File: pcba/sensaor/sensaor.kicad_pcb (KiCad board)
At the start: 2 copper layers, 26 x 77 mm, 16 parts, among them J1 SAO, J2 WS2812, J3 Conn_01x05_Pin, J4 Conn_01x05_Pin, J5 Conn_01x05_Pin, J6 Programming, J7 Conn_01x05_Pin, J8 Conn_01x05_Pin, J9 Conn_01x05_Pin, U1 CH32V003AxMx

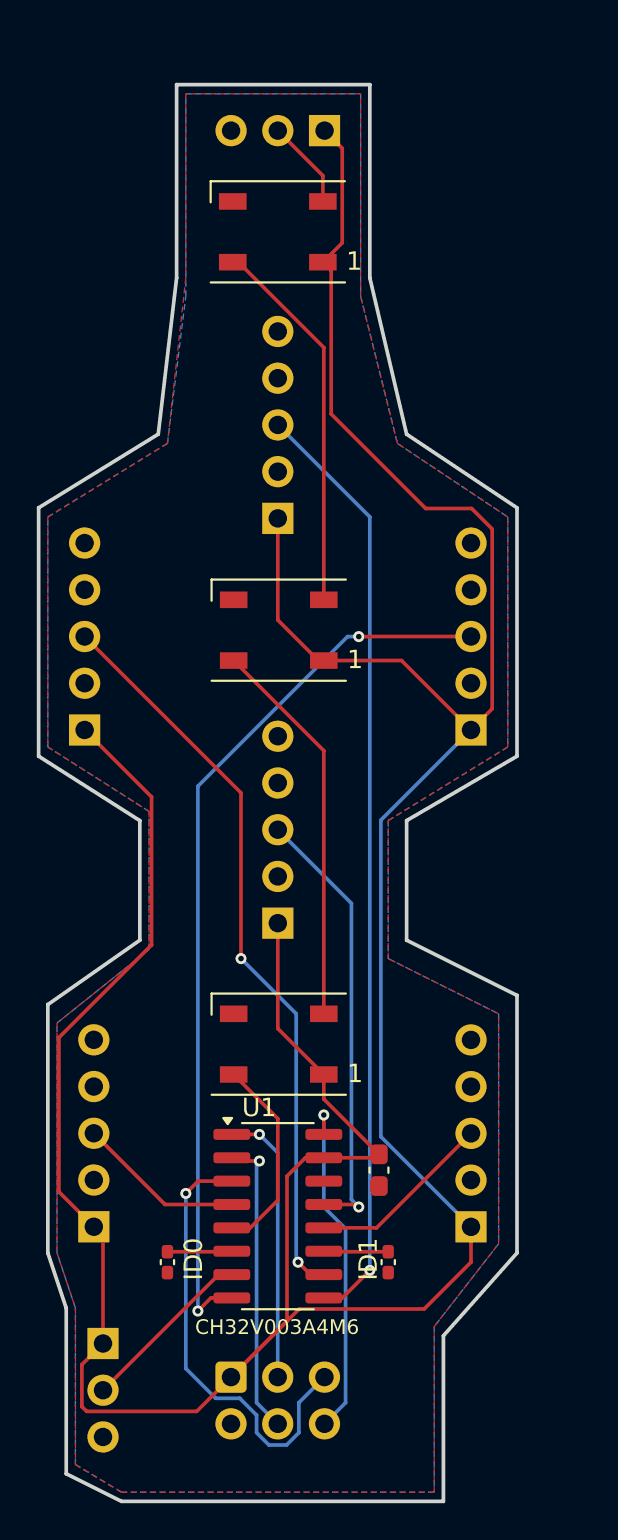
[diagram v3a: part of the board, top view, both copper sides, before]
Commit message: Add SAOAO connector, tweak some placements
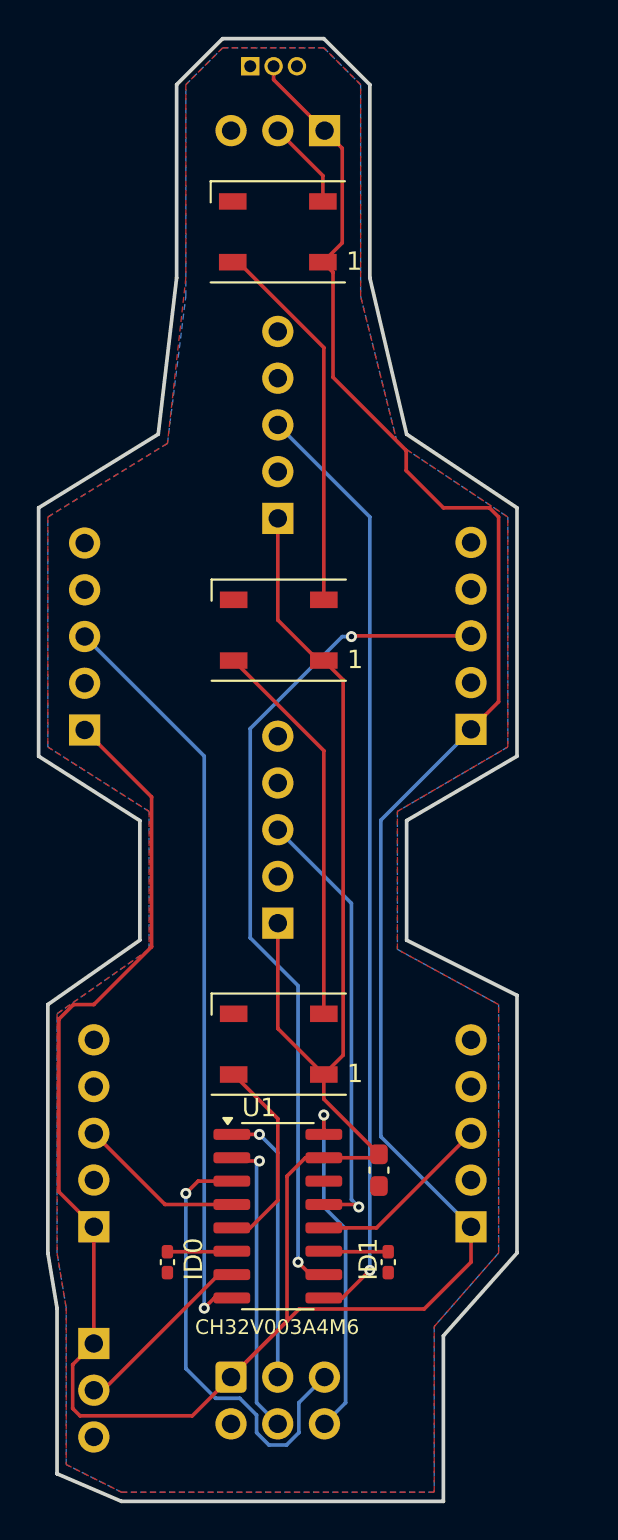
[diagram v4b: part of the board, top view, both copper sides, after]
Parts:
- added J10: SAOAO, Connector_PinHeader_1.27mm:PinHeader_1x03_P1.27mm_Vertical, B.Cu at (92.0, 17.0)
- moved J7 21.0 mm to (104.0, 53.0)
- moved J9 21.0 mm to (83.0, 53.1)
- moved J6 0.50 mm to (83.5, 86.4)
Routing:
- net VCC: track 190.5 -> 210.4 mm
- net /AB: track 48.9 -> 40.9 mm, vias 2 -> 1
- net /AR: track 40.5 -> 45.8 mm
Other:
- board size 26 x 77 mm -> 26 x 79.5 mm

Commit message: Adjustments from PCBA review
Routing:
- net VCC: track 210.4 -> 212.4 mm
- net /AR: track 45.8 -> 46.9 mm
- net Net-(D1-DOUT): track 21.2 -> 21.9 mm
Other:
- outline, holes or cut-outs redrawn

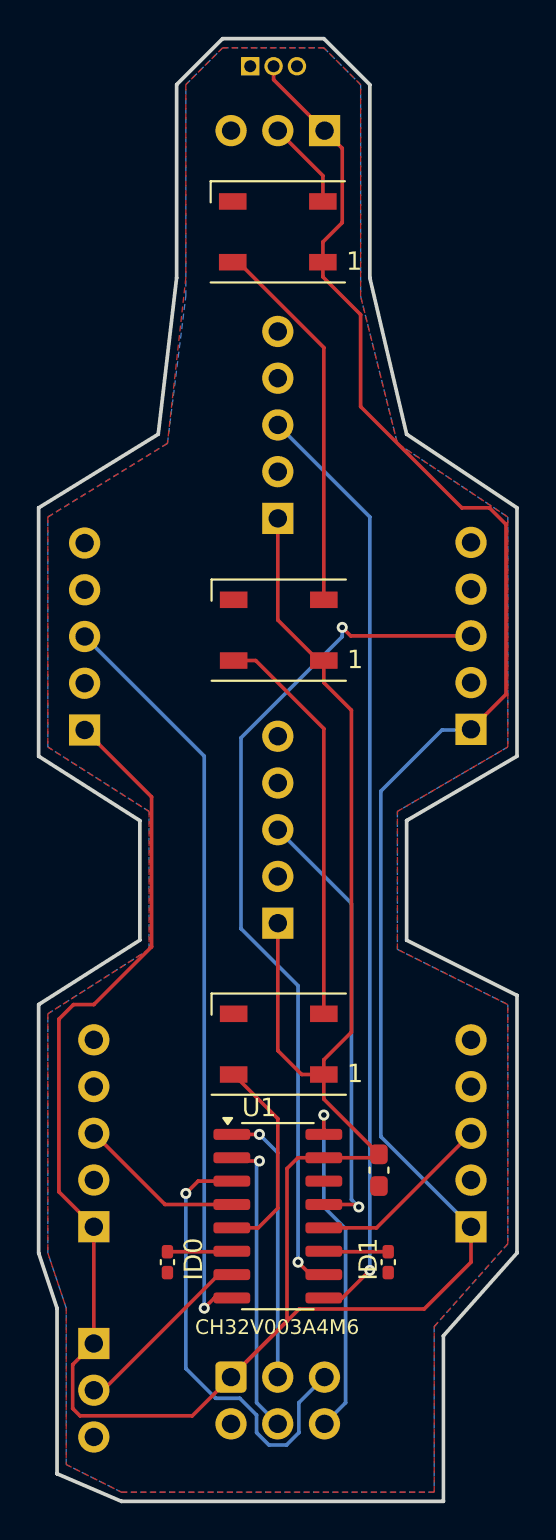
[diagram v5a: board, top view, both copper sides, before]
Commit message: Adjusted layout. Ordered 30x v1.0 boards
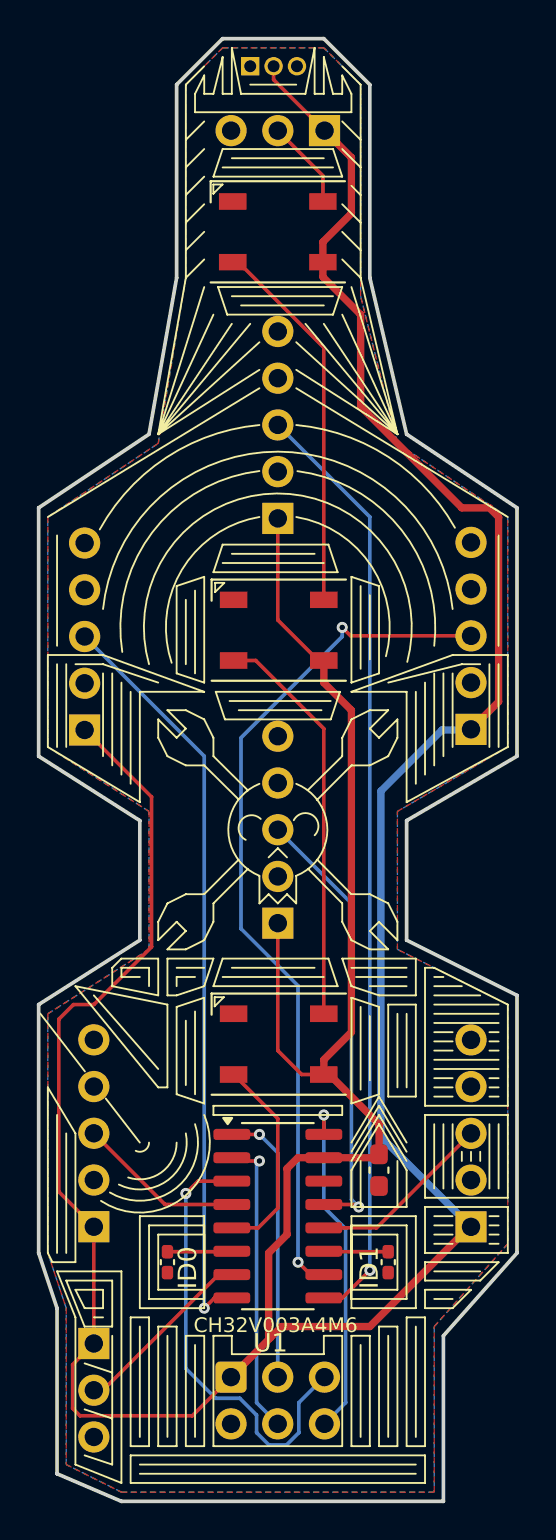
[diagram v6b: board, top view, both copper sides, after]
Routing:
- net VCC: track 212.4 -> 208.6 mm
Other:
- outline, holes or cut-outs redrawn
- board text added: "GPIO1 SDA 3.3V GPIO2 SCL GND"
